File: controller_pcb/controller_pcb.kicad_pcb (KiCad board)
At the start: 2 copper layers, 64.5 x 53.5 mm, 29 parts, among them IC1 AMS1117-5.0, J1 A_08-LC-TT, J2 SM04B-GHS-TB_LF__SN_, Q1 SI2301CDS-T1-GE3.

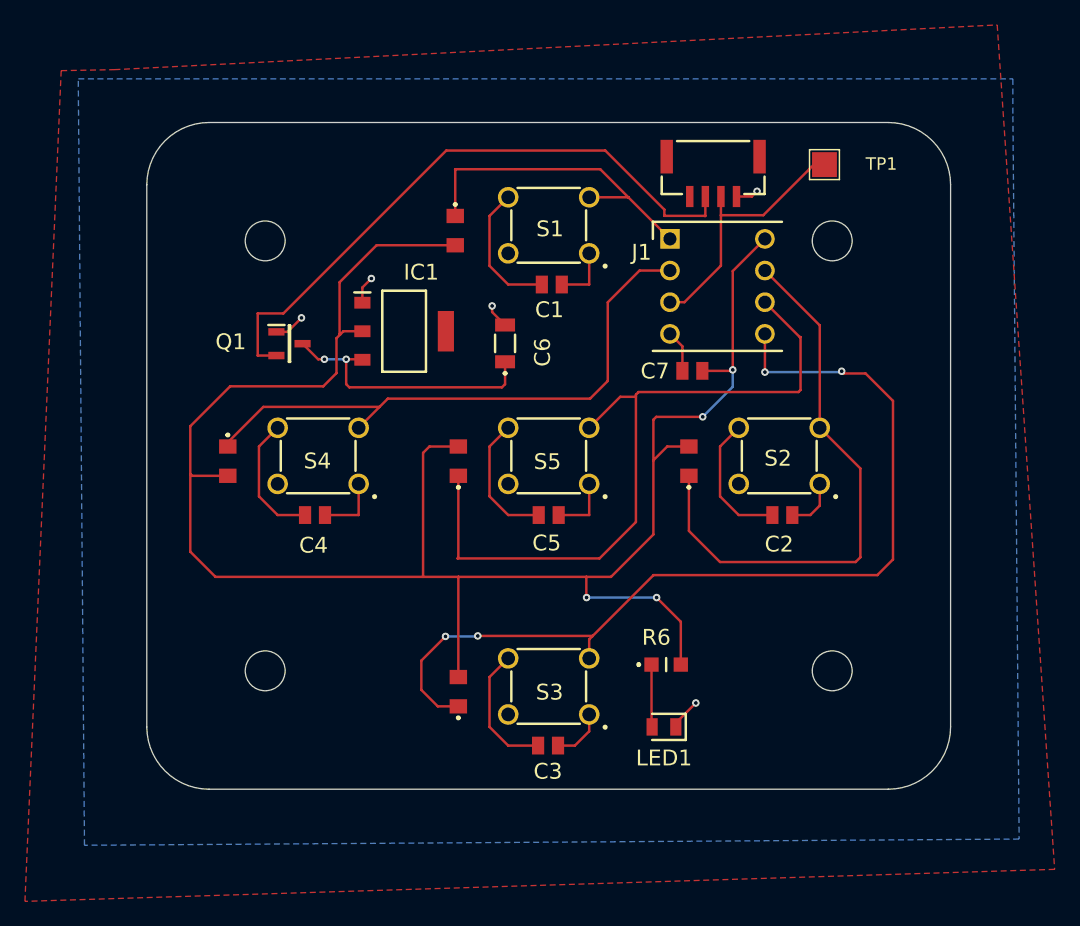
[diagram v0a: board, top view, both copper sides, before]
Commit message: added hirose DF13 to check footprints
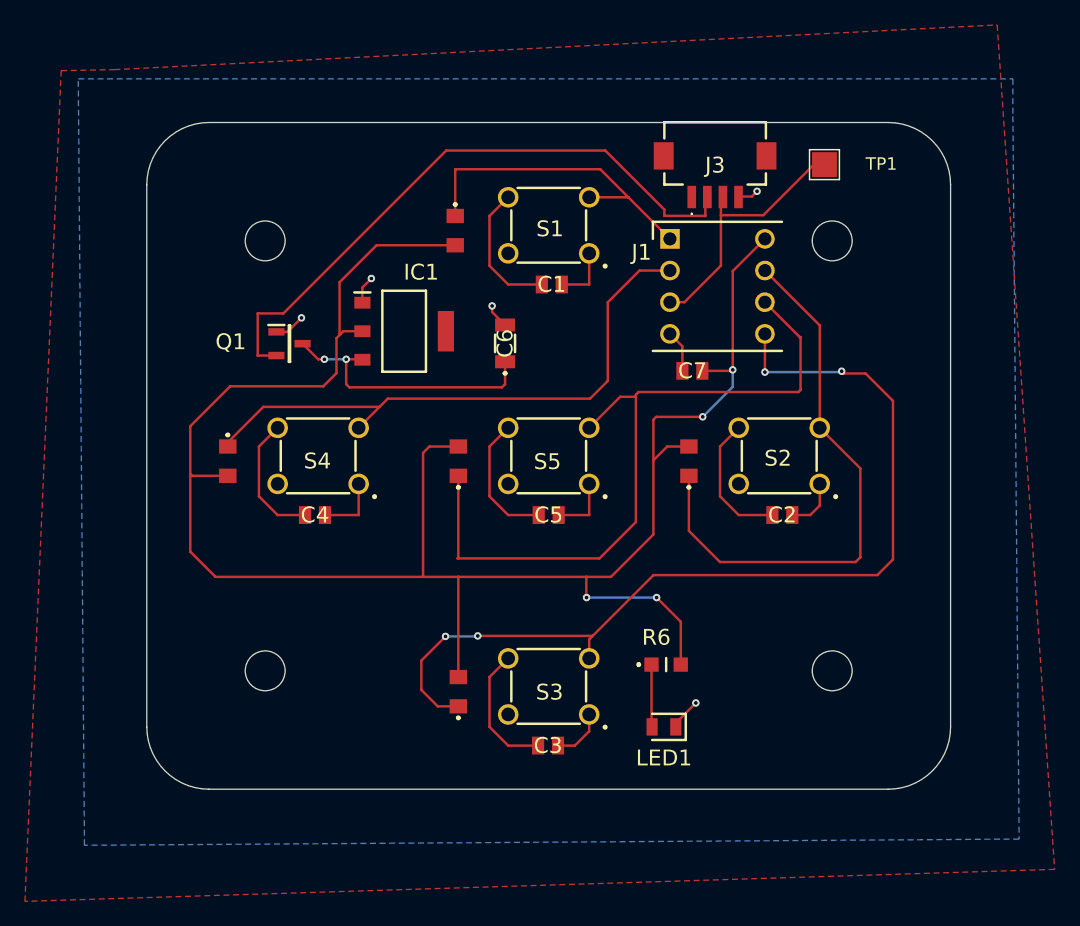
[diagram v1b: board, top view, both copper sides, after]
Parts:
- removed J2: SM04B-GHS-TB_LF__SN_, Controller_Footprints:SM04B-GHS-TB
- added J3: DF13-4P-1.25H_21_, Controller_Footprints:DF134P125H21, F.Cu at (146.6, 103.0)
- C7: footprint Library:CAPC2012X140N -> Controller_Footprints:CAPC2012X140N
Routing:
- net unconnected-(J3-Pad4): track 0.00 -> 1.82 mm, vias 0 -> 1
- net GND: track 14.5 -> 12.6 mm, vias 5 -> 4

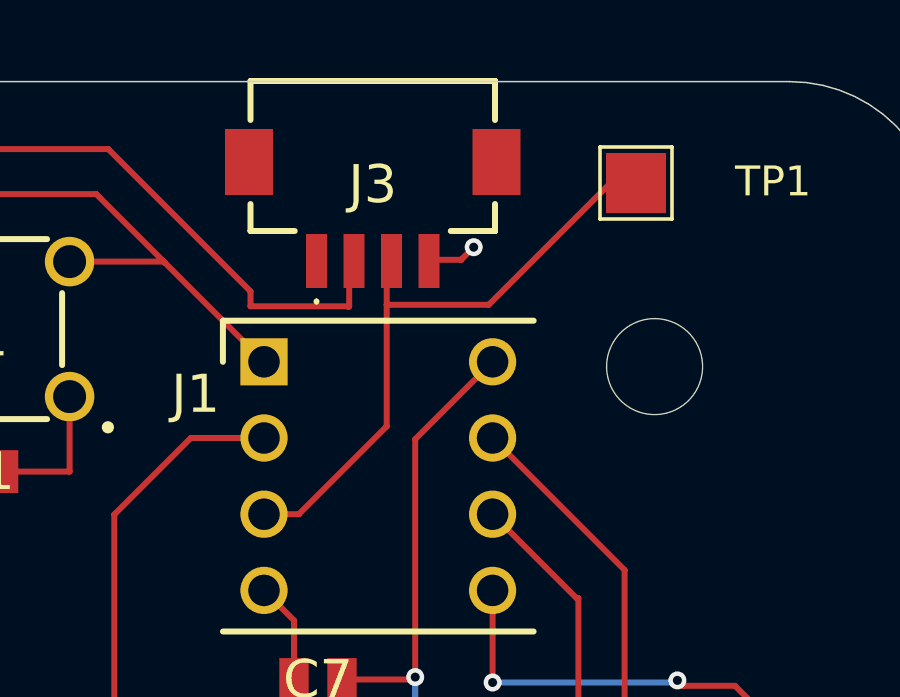
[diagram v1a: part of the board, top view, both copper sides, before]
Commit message: updated wiring and copper fill
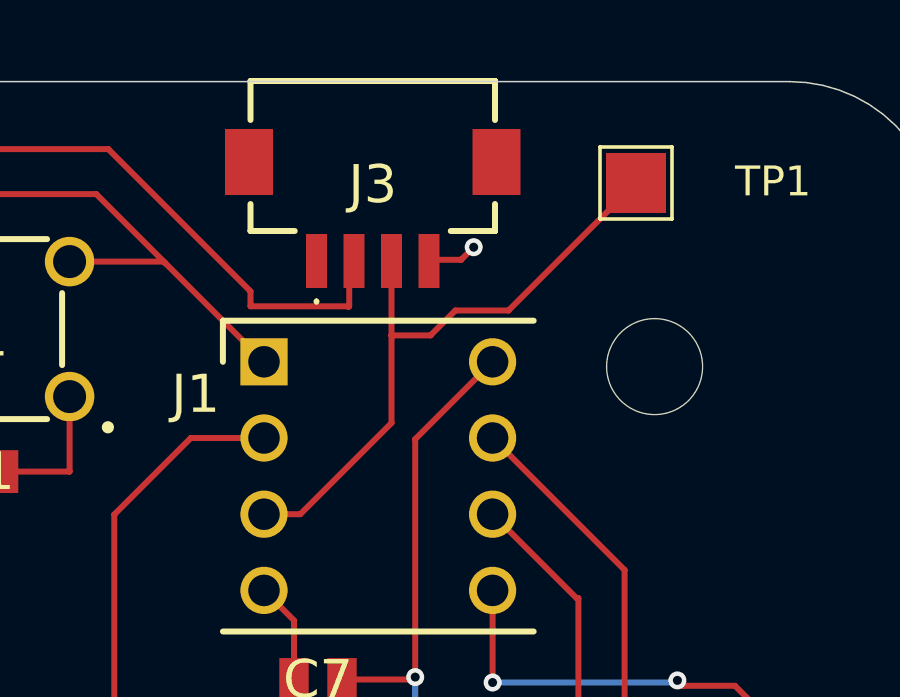
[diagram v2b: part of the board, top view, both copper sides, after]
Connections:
- J3 pad 1: Net-(J1-Pad3) -> unconnected-(J3-Pad1)
- J3 pad 3: GND -> Net-(J1-Pad3)
- J3 pad 4: unconnected-(J3-Pad4) -> GND
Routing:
- net unconnected-(J3-Pad4): track 1.82 -> 0.00 mm, vias 1 -> 0
- net GND: track 12.6 -> 14.5 mm, vias 4 -> 5
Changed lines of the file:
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@@
 	(net 23 "unconnected-(J3-PadMP1)")
 	(net 24 "unconnected-(J3-PadMP2)")
-	(net 25 "unconnected-(J3-Pad4)")
+	(net 25 "unconnected-(J3-Pad1)")
 	(footprint "Controller_Footprints:CAPC2012X140N"
 		(layer "F.Cu")
@@
 			(size 0.7 1.8)
 			(layers "F.Cu" "F.Mask" "F.Paste")
-			(net 15 "Net-(J1-Pad3)")
+			(net 25 "unconnected-(J3-Pad1)")
 			(pinfunction "1")
 			(pintype "passive")
@@
 			(size 0.7 1.8)
 			(layers "F.Cu" "F.Mask" "F.Paste")
-			(net 11 "GND")
+			(net 15 "Net-(J1-Pad3)")
 			(pinfunction "3")
 			(pintype "passive")
@@
 			(size 0.7 1.8)
 			(layers "F.Cu" "F.Mask" "F.Paste")
-			(net 25 "unconnected-(J3-Pad4)")
+			(net 11 "GND")
 			(pinfunction "4")
 			(pintype "passive")
@@
 	)
 	(segment
+		(start 149.55 106.44)
+		(end 149.97 106.02)
+		(width 0.2)
+		(layer "F.Cu")
+		(net 11)
+	)
+	(segment
+		(start 148.32 106.44)
+		(end 149.55 106.44)
+		(width 0.2)
+		(layer "F.Cu")
+		(net 11)
+	)
+	(segment
 		(start 145.06 147.08)
 		(end 143.45 148.69)
@@
 	)
 	(via
+		(at 149.97 106.02)
+		(size 0.6)
+		(drill 0.3)
+		(layers "F.Cu" "B.Cu")
+		(net 11)
+	)
+	(via
 		(at 128.71 115.22)
 		(size 0.6)
@@
 	)
 	(segment
-		(start 147.07 107.94)
-		(end 147.07 111.99)
+		(start 149.36 108.13)
+		(end 151.13 108.13)
+		(width 0.2)
+		(layer "F.Cu")
+		(net 15)
+	)
+	(segment
+		(start 147.23 108.96)
+		(end 148.53 108.96)
 		(width 0.2)
 		(layer "F.Cu")
@@
 	)
 	(segment
-		(start 155.38 103.88)
-		(end 154.53 103.88)
+		(start 147.23 108.96)
+		(end 147.23 106.48)
 		(width 0.2)
 		(layer "F.Cu")
@@
 	)
 	(segment
-		(start 150.47 107.94)
-		(end 147.07 107.94)
+		(start 151.13 108.13)
+		(end 155.38 103.88)
 		(width 0.2)
 		(layer "F.Cu")
@@
 	)
 	(segment
-		(start 147.07 107.94)
-		(end 147.07 106.44)
+		(start 142.98 114.92)
+		(end 144.19 114.92)
 		(width 0.2)
 		(layer "F.Cu")
@@
 	)
 	(segment
-		(start 144.14 114.92)
-		(end 142.98 114.92)
+		(start 147.23 111.88)
+		(end 147.23 108.96)
 		(width 0.2)
 		(layer "F.Cu")
@@
 	)
 	(segment
-		(start 147.07 111.99)
-		(end 144.14 114.92)
+		(start 148.53 108.96)
+		(end 149.36 108.13)
 		(width 0.2)
 		(layer "F.Cu")
@@
 	)
 	(segment
-		(start 154.53 103.88)
-		(end 150.47 107.94)
+		(start 144.19 114.92)
+		(end 147.23 111.88)
 		(width 0.2)
 		(layer "F.Cu")
@@
 		(net 22)
 	)
-	(segment
-		(start 149.55 106.44)
-		(end 149.97 106.02)
-		(width 0.2)
-		(layer "F.Cu")
-		(net 25)
-	)
-	(segment
-		(start 148.32 106.44)
-		(end 149.55 106.44)
-		(width 0.2)
-		(layer "F.Cu")
-		(net 25)
-	)
-	(via
-		(at 149.97 106.02)
-		(size 0.6)
-		(drill 0.3)
-		(layers "F.Cu" "B.Cu")
-		(net 25)
-	)
 	(zone
